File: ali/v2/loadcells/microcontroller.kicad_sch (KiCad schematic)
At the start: 41 parts, among them J1 Conn_02x01, J2 Conn_01x05, J3 USB_C_Receptacle_USB2.0_16P, J4 Conn_01x15, J5 Conn_02x09_Counter_Clockwise, J6 Screw_Terminal_01x02, SW1 SKRPANE010, U1 STM32H563RIV6, U2 AP2112K-3.3, Y1 25 MHz

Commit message: mfw tcs
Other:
- note added: "GPIO"
- note added: "POWER"
- note removed: "GPIO Banks"
- moved on the sheet: C1, C10, C11, C12, C13, C14, C15, C16, C17, C2, C3, C4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

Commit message: Update load cells to use timer pins
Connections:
- net +3.3V: now also J4.12 (Pin_12); no longer J4.11 (Pin_11)
- net ADC_CS: now also U1.3 (PC14); no longer U1.60 (PB6)
- net ADC_DRDY: now also U1.57 (PB3(JTDO); no longer U1.56 (PC12)
- net ADC_RESET: now also U1.2 (PC13); no longer U1.3 (PC14)
- net ADC_START: now also U1.4 (PC15); no longer U1.61 (PB7)
- net GND: no longer J4.15 (Pin_15)
- net USER_LED_1: now also U1.38 (PD11); no longer U1.26 (PB0)
- net USER_LED_2: now also U1.39 (PD12); no longer U1.27 (PB1)
- net USER_LED_3: now also U1.40 (PC6); no longer U1.28 (PB2)
- net MISO renamed ADC_MISO
- net ADC_MISO: now also J4.10 (Pin_10); no longer J4.8 (Pin_8)
- net MOSI renamed ADC_MOSI
- net ADC_MOSI: now also J4.11 (Pin_11); no longer J4.9 (Pin_9)
- net PA15 renamed TIM2_CH1
- net PA3 renamed TIM2_CH4
- net PA5 renamed ADC_SCLK
- net ADC_SCLK: now also J4.9 (Pin_9); no longer J5.5 (Pin_5)
- net PB10 renamed PB2
- net PB2: now also U1.28 (PB2); no longer U1.29 (PB10)
- net PB8 renamed I2C1_SCA
- net I2C1_SCA: now also U1.61 (PB7); no longer U1.63 (PB8)
- net PB9 renamed UART4_TX
- net PC10: no longer names the net of U1.54 (PC10)
- net PC10: no longer J4.13 (Pin_13)
- net PC11: no longer names the net of U1.55 (PC11)
- net PC11: no longer J4.12 (Pin_12)
- net PE0: no longer names the net of U1.65 (PE0)
- net PE0: no longer J4.6 (Pin_6)
- removed net SCLK: J4.10 (Pin_10), U1.57 (PB3(JTDO)
- new net I2C1_SCL: J4.8 (Pin_8), U1.60 (PB6)
- new net PB0: J5.5 (Pin_5), U1.26 (PB0)
- new net PC12: J4.13 (Pin_13), U1.56 (PC12)
- new net TIM2_CH3: J4.15 (Pin_15), U1.29 (PB10)
- new net UART4_RX: J4.6 (Pin_6), U1.63 (PB8)
- no-connect marks 18 -> 17
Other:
- moved on the sheet: D1, D2, R3, R4

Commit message: Swap to sync'd ADS1261s on LC, update README and clean up Just scripts, some frame changes too.
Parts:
- added C12: 100nF, APRL_Passive:C_0603, symbol Device:C_Small
- added Y2: 7.3278 MHz, APRL_Passive:Oscillator_SCTF_SX3M_3.2x2.5mm, symbol APRL_Misc:SX3M-xxxMHz
- renumbered C12 to C13, C13 to C14, C14 to C15, C15 to C16, C16 to C17, C17 to C18, D3 to D1, D4 to D2, D1 to D3, D2 to D4, R5 to R3, R3 to R4, R4 to R5
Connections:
- net ADC_CS is gone; now on net ADC_START: U1.3 (PC14)
- net +3.3V: now also C12.1, Y2.1 (EN), Y2.4 (Vdd)
- net ADC_RESET: now also U1.4 (PC15); no longer U1.2 (PC13)
- net ADC_START: no longer U1.4 (PC15)
- net GND: now also C12.2, Y2.2 (GND)
- net PA4: now also J5.15 (Pin_15); no longer J5.7 (Pin_7)
- net PA6: now also J5.11 (Pin_11); no longer J5.3 (Pin_3)
- net PB0: now also J5.13 (Pin_13); no longer J5.5 (Pin_5)
- net PB2: now also J5.9 (Pin_9); no longer J5.17 (Pin_17)
- net TIM2_CH4: now also J5.17 (Pin_17); no longer J5.9 (Pin_9)
- net USER_LED_1: now also U1.39 (PD12); no longer U1.38 (PD11)
- net USER_LED_2: now also U1.40 (PC6); no longer U1.39 (PD12)
- net USER_LED_3: now also U1.41 (PC7); no longer U1.40 (PC6)
- net PB13: now reaches U1.35 (PB13)
- net PB13: now also J5.7 (Pin_7)
- net PB14: now reaches U1.36 (PB14)
- net PB14: now also J5.5 (Pin_5)
- net PC0 renamed ADC2_CS
- net ADC2_CS: no longer J5.15 (Pin_15)
- net PC2 renamed ADC3_CS
- net ADC3_CS: no longer J5.13 (Pin_13)
- net PC3 renamed ADC4_CS
- net ADC4_CS: no longer J5.11 (Pin_11)
- new net ADC1_CS: U1.2 (PC13)
- new net ADC_CLK: Y2.3 (OUT)
- new net PD11: J5.3 (Pin_3), U1.38 (PD11)
- no-connect marks 17 -> 14
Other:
- note added: "ADC OSC"
- moved on the sheet: D3, D4, J4, J5, R4, R5
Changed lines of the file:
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@@
 	(title_block
 		(date "2026-09-11")
-		(rev "1A")
 	)

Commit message: Minor thermocouple updates
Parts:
- added R28: 22R, APRL_Passive:R_0603, symbol Device:R_Small_US
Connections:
- net ADC_CLK: now also R28.2; no longer Y2.3 (OUT)
- new net: R28.1, Y2.3 (OUT)
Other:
- note added: "Smaller CMOS crystals have undefined minimum rise times, so we're placing a series termination resistor just in case"

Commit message: Globally remove LCSC labels, update MPNs and IOCs, add +5V monitoring to DAQs, fix some footprints
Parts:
- added R7, R9: 10k, APRL_Passive:R_0603, symbol Device:R_Small_US
- J5: MANUFACTURER Molex -> (none); MPN 503159-1501 -> (none)
- R10: renamed from R28; MPN (none) -> RC0603FR-0722RL
- Y2: value 7.3278 MHz -> 7.3728 MHz; MANUFACTURER (none) -> SCTF
- renumbered D3 to D1, D4 to D2, D1 to D3, D2 to D4, R4 to R3, R5 to R4, R3 to R5, R7 to R8
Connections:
- net +5V: now also R7.1
- net GND: now also R9.2
- net PA6: now also J5.13 (Pin_13); no longer J5.11 (Pin_11)
- net PB0: now also J5.11 (Pin_11); no longer J5.13 (Pin_13)
- net +5V_SENSE: now reaches U1.27 (PB1)
- net +5V_SENSE: now also R7.2, R9.1
- no-connect marks 14 -> 13
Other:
- moved on the sheet: D1, D2, R3, R4

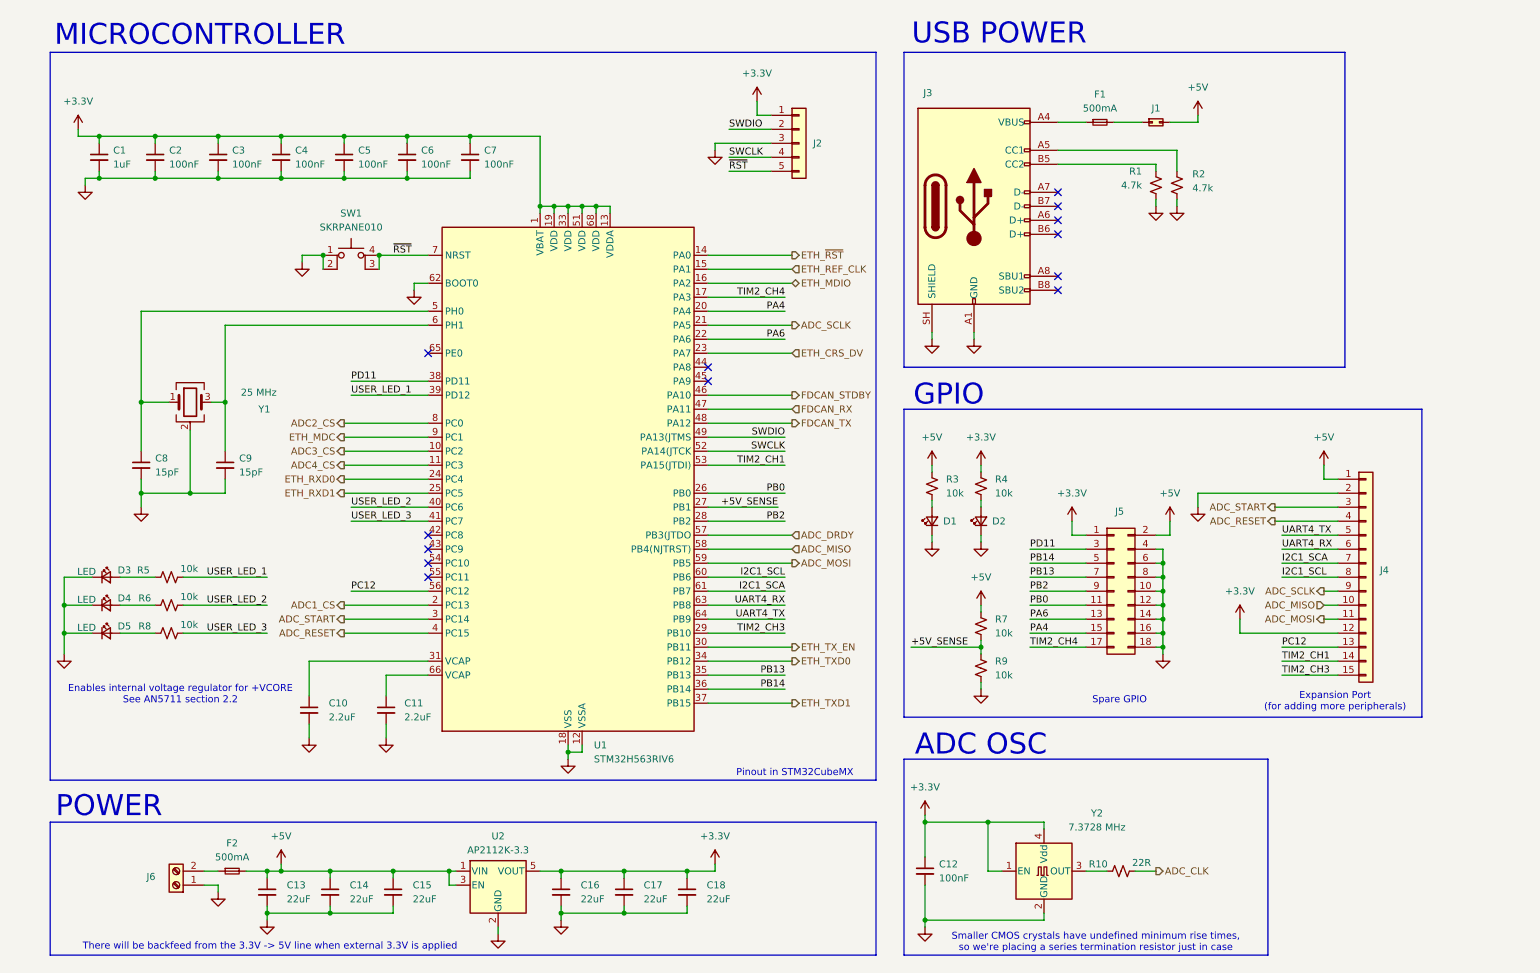
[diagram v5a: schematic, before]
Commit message: the great flatpak and kicad 10.0.6 migration
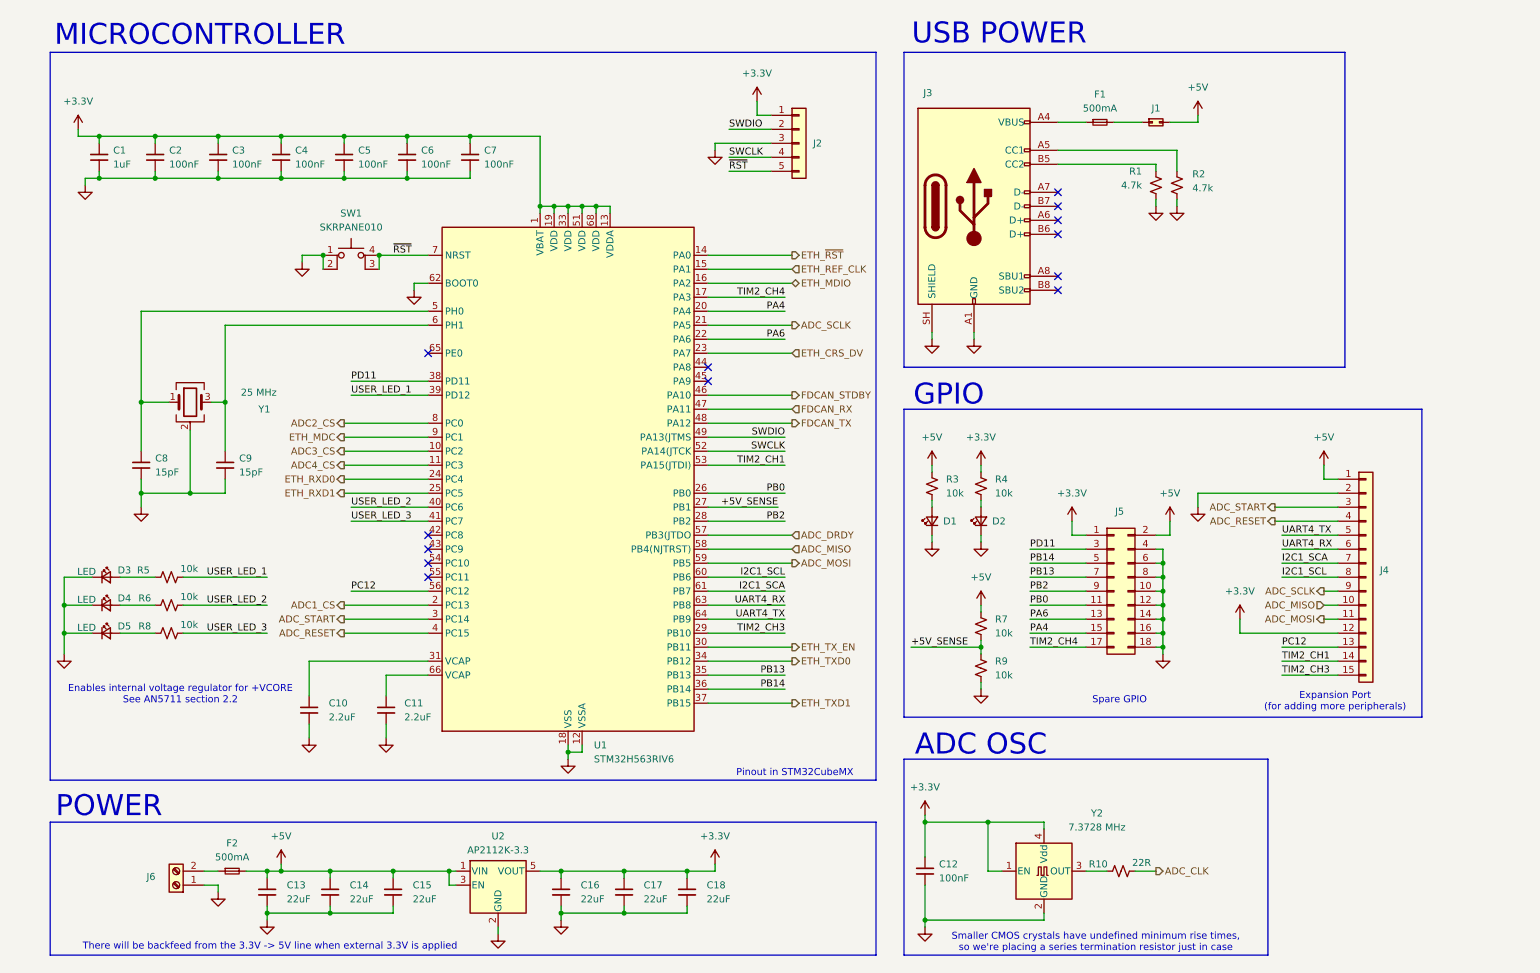
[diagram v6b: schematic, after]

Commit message: The other half of the great 10.0.6 migration
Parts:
- U1: symbol MCU_ST_STM32H5:STM32H563RIVx -> APRL_MCU:STM32H563RIVx
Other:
- note added: "I2C is broken out but no pullups on host side"

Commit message: Add more commentary
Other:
- note added: "This spare GPIO header is not standardized, its literally just whatever I had available just so that we'd have it available if we ever needed it"
